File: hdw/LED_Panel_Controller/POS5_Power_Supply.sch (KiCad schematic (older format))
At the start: 20 parts

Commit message: lots of schematic progress
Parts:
- C?: display_footprint (none) -> 0402
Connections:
- net +5V: now also Q?.3 (D)
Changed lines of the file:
@@
 encoding utf-8
 Sheet 6 34
-Title "Pulse Oximeter"
-Date "2020-08-01"
+Title "LED Panel Controller"
+Date "2020-12-23"
 Rev "A"
-Comp "Drew Maatman"
+Comp "Drew Maatman, Logan Wedel"
 Comment1 ""
 Comment2 ""
@@
 F 2 "Capacitors_SMD:C_0402" H 4228 4620 50  0001 C CNN
 F 3 "" H 4215 4870 50  0001 C CNN
-F 4 "" H 4040 4870 50  0000 R CNN "display_footprint"
+F 4 "0402" H 4040 4870 50  0000 R CNN "display_footprint"
 F 5 "50V" H 4040 4770 50  0000 R CNN "Voltage"
 F 6 "X7R" H 4040 4670 50  0000 R CNN "Dielectric"
@@
 	-1   0    0    1
 $EndComp
+$Comp
+L power:+5V #PWR?
+U 1 1 5FE45BF8
+P 5120 7010
+F 0 "#PWR?" H 5120 6860 50  0001 C CNN
+F 1 "+5V" H 5120 7150 50  0000 C CNN
+F 2 "" H 5120 7010 50  0001 C CNN
+F 3 "" H 5120 7010 50  0001 C CNN
+	1    5120 7010
+	1    0    0    -1
+$EndComp
 $EndSCHEMATC

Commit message: made a lot more schematic progress
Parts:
- removed R?: 0.02, Resistors_SMD:R_0612, symbol Custom_Library:R_Custom
- removed R? (x2): 10, Resistors_SMD:R_0402, symbol Custom_Library:R_Custom
- added R? (x2): 10, Resistors_SMD:R_0402, symbol Custom_Library:R_Custom
- added R? (x3): 0, Resistors_SMD:R_0402, symbol Custom_Library:R_Custom
- added R?: 0.02, Resistors_SMD:R_0612, symbol Custom_Library:R_Custom
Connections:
- net +5V: now also R?.2, R?.2, R?.2, R?.2, R?.2
- net POS5_SNS_OUT+: now also R?.1
- net POS5_SNS_OUT-: now also R?.1
- net at C?.1, L?.2: now also R?.1, R?.1, R?.1, R?.1, R?.2

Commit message: more schematic development
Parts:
- removed C?: 100uF, symbol Custom_Library:C_Custom
- removed C?: 0.1uF, Capacitors_SMD:C_0402, symbol Custom_Library:C_Custom
- removed C?: 10uF, Capacitors_SMD:C_0402, symbol Custom_Library:C_Custom
- removed D?: BAT48JFILM, Diode_SMD:D_SOD-323, symbol Diode:BAT48JFILM
- removed L?: 2.2uH, symbol Custom_Library:L_Custom
- removed Q?: ZXMS6004FFTA, Package_TO_SOT_SMD:SOT-23, symbol Custom_Library:ZXMS6004FFTA
- removed Q?: BSS214NW, Package_TO_SOT_SMD:SOT-323_SC-70, symbol Transistor_FET:BSS214NW
- removed R?: 953k, Resistors_SMD:R_0402, symbol Custom_Library:R_Custom
- removed R? (x2): 10k, Resistors_SMD:R_0402, symbol Custom_Library:R_Custom
- removed R? (x2): 10, Resistors_SMD:R_0402, symbol Custom_Library:R_Custom
- removed R? (x3): 0, Resistors_SMD:R_0402, symbol Custom_Library:R_Custom
- removed R?: 0.02, Resistors_SMD:R_0612, symbol Custom_Library:R_Custom
- removed U?: TPS62130, Package_DFN_QFN:QFN-16-1EP_3x3mm_P0.5mm_EP1.8x1.8mm, symbol Custom_Library:TPS62130
- added C?: 0.1uF, Capacitors_SMD:C_0402, symbol Custom_Library:C_Custom
- added C? (x2): 10uF, Capacitors_SMD:C_1206, symbol Custom_Library:C_Custom
- added C?: 10uF, Capacitors_SMD:C_0402, symbol Custom_Library:C_Custom
- added D?: BAT48JFILM, Diode_SMD:D_SOD-323, symbol Diode:BAT48JFILM
- added L?: 2.2uH, symbol Custom_Library:L_Custom
- added Q?: ZXMS6004FFTA, Package_TO_SOT_SMD:SOT-23, symbol Custom_Library:ZXMS6004FFTA
- added Q?: BSS214NW, Package_TO_SOT_SMD:SOT-323_SC-70, symbol Transistor_FET:BSS214NW
- added R?: 0.02, Resistors_SMD:R_0612, symbol Custom_Library:R_Custom
- added R? (x2): 10, Resistors_SMD:R_0402, symbol Custom_Library:R_Custom
- added R? (x4): 0, Resistors_SMD:R_0402, symbol Custom_Library:R_Custom
- added R? (x3): 10k, Resistors_SMD:R_0402, symbol Custom_Library:R_Custom
- added R?: 953k, Resistors_SMD:R_0402, symbol Custom_Library:R_Custom
- added U?: 74LVC1G97, Package_TO_SOT_SMD:SOT-363_SC-70-6, symbol Custom_Library:74LVC1G97_Power_AND
- added U?: TPS62133, Package_DFN_QFN:QFN-16-1EP_3x3mm_P0.5mm_EP1.8x1.8mm, symbol Custom_Library:TPS62130
- C?: Dielectric X7R -> X5R; Digi-Key PN 1276-7031-1-ND -> 1276-1181-1-ND
- C?: Digi-Key PN (none) -> 490-10698-1-ND; Voltage 50V -> 25V
- C?: Digi-Key PN 490-13295-1-ND -> 399-3066-1-ND
- R?: Configuration (none) -> DNP; Digi-Key PN (none) -> RMCF0402FT180KCT-ND
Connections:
- net +12V: now also U?.10 (AVIN), U?.11 (PVIN), U?.12 (PVIN)
- net +3V3: now also R?.1, C?.1, D?.2 (A), U?.5 (VCC)
- net +5V: now also Q?.3 (D), R?.1, R?.2, R?.2, R?.2, R?.2, R?.2, U?.14 (VOS)
- net GND: now also C?.2, C?.2, C?.2, C?.2, Q?.2 (S), Q?.2 (S), R?.2, R?.2, R?.2, U?.1 (GND), U?.15 (PGND), U?.16 (PGND), U?.17 (EP), U?.2 (GND), U?.6 (AGND), U?.7 (FSW), U?.8 (DEF); no longer R?.2
- net POS5_PGOOD: now also R?.1, U?.4
- net POS5_RUN: now also Q?.1 (G), R?.1, U?.13 (EN), U?.3; no longer R?.1
- net at R?.1: now also R?.1, R?.2, U?.5 (FB)
- net at C?.1: now also U?.9 (SS/TR)
- new net: C?.1, C?.1, L?.2, R?.1, R?.1, R?.1, R?.1, R?.2
- new net: R?.2, U?.4 (PG), U?.6
- new net: L?.1, U?.1 (SW), U?.2 (SW), U?.3 (SW)
- new net: Q?.1 (G), Q?.3 (D), R?.2
- new net: C?.1, D?.1 (K), R?.1
- new net POS5_SNS+: R?.1
- new net POS5_SNS-: R?.1
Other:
- note added: "Fixed VOUT = +5V"
- moved on the sheet: R?, TP?

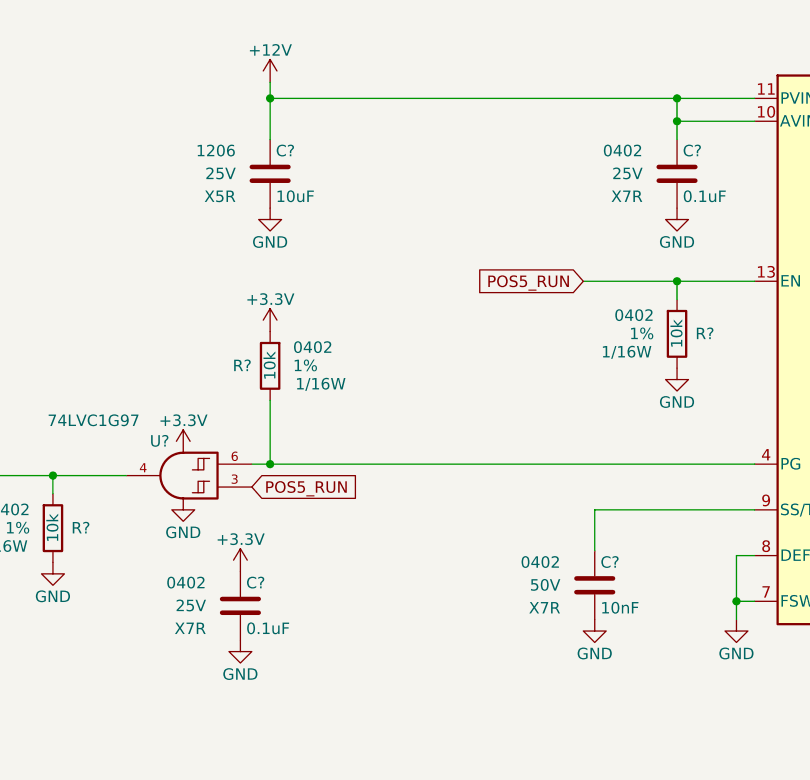
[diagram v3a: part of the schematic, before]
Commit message: added digikey pns, footprints, bom scrubbed
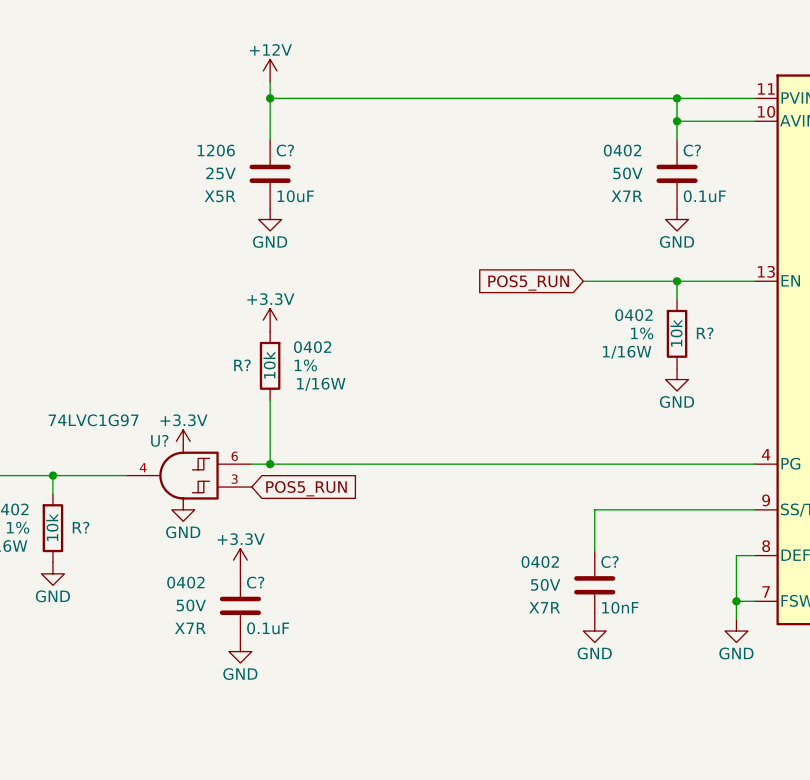
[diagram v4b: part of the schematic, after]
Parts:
- C? (x3): Digi-Key PN 1276-1181-1-ND -> 399-8153-1-ND
- C? (x2): Digi-Key PN 490-10698-1-ND -> 490-10701-1-ND; Voltage 25V -> 50V
- C?: Digi-Key PN 490-13211-1-ND -> 1276-1451-1-ND
- L?: footprint (none) -> Inductors_SMD:L_Vishay_IHLP-2020
- R? (x4): Digi-Key PN 2019-RK73Z1ETTPCT-ND -> RMCF0402ZT0R00CT-ND
- R?: Digi-Key PN (none) -> RMCF0402FT953KCT-ND
- U?: Digi-Key PN 296-SN74LVC1G97DCK3CT-ND -> 1727-1772-1-ND
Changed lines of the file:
@@
 F 3 "" H 4575 3070 50  0001 C CNN
 F 4 "0402" H 4400 3070 50  0000 R CNN "display_footprint"
-F 5 "25V" H 4400 2970 50  0000 R CNN "Voltage"
+F 5 "50V" H 4400 2970 50  0000 R CNN "Voltage"
 F 6 "X7R" H 4400 2870 50  0000 R CNN "Dielectric"
-F 7 "490-10698-1-ND" H 4550 2970 50  0001 C CNN "Digi-Key PN"
+F 7 "490-10701-1-ND" H 4550 2970 50  0001 C CNN "Digi-Key PN"
 	1    4550 2970
 	1    0    0    -1
@@
 F 5 "25V" H 2620 2970 50  0000 R CNN "Voltage"
 F 6 "X5R" H 2620 2870 50  0000 R CNN "Dielectric"
-F 7 "1276-1181-1-ND" H 3195 3470 60  0001 C CNN "Digi-Key PN"
+F 7 "399-8153-1-ND" H 3195 3470 60  0001 C CNN "Digi-Key PN"
 	1    2770 2970
 	1    0    0    -1
@@
 F 2 "Package_TO_SOT_SMD:SOT-363_SC-70-6" H 2440 4290 50  0001 C CNN
 F 3 "http://www.ti.com/lit/ds/symlink/sn74lvc1g97.pdf" H 2440 4290 50  0001 C CNN
-F 4 "296-SN74LVC1G97DCK3CT-ND" H 2390 4290 50  0001 C CNN "Digi-Key PN"
+F 4 "1727-1772-1-ND" H 2390 4290 50  0001 C CNN "Digi-Key PN"
 	1    2390 4290
 	-1   0    0    -1
@@
 F 3 "" H 2665 4960 50  0001 C CNN
 F 4 "0402" H 2490 4960 50  0000 R CNN "display_footprint"
-F 5 "25V" H 2490 4860 50  0000 R CNN "Voltage"
+F 5 "50V" H 2490 4860 50  0000 R CNN "Voltage"
 F 6 "X7R" H 2490 4760 50  0000 R CNN "Dielectric"
-F 7 "490-10698-1-ND" H 2640 4860 50  0001 C CNN "Digi-Key PN"
+F 7 "490-10701-1-ND" H 2640 4860 50  0001 C CNN "Digi-Key PN"
 	1    2640 4860
 	1    0    0    -1
@@
 F 5 "1%" H 7310 4720 50  0000 R CNN "Tolerance"
 F 6 "1/16W" H 7310 4620 50  0000 R CNN "Wattage"
-F 7 "2019-RK73Z1ETTPCT-ND" H 7410 4720 50  0001 C CNN "Digi-Key PN"
+F 7 "RMCF0402ZT0R00CT-ND" H 7410 4720 50  0001 C CNN "Digi-Key PN"
 	1    7410 4720
 	-1   0    0    -1
@@
 F 6 "1/16W" V 8310 3450 50  0001 C CNN "Wattage"
 F 7 "~Telemetry" V 8110 3450 50  0000 C CNN "Configuration"
-F 8 "2019-RK73Z1ETTPCT-ND" H 8010 3450 50  0001 C CNN "Digi-Key PN"
+F 8 "RMCF0402ZT0R00CT-ND" H 8010 3450 50  0001 C CNN "Digi-Key PN"
 	1    8010 3450
 	0    -1   1    0
@@
 F 6 "1/16W" V 8310 3750 50  0001 C CNN "Wattage"
 F 7 "~Telemetry" V 8110 3750 50  0000 C CNN "Configuration"
-F 8 "2019-RK73Z1ETTPCT-ND" H 8010 3750 50  0001 C CNN "Digi-Key PN"
+F 8 "RMCF0402ZT0R00CT-ND" H 8010 3750 50  0001 C CNN "Digi-Key PN"
 	1    8010 3750
 	0    -1   1    0
@@
 F 6 "1/16W" V 8310 4050 50  0001 C CNN "Wattage"
 F 7 "~Telemetry" V 8110 4050 50  0000 C CNN "Configuration"
-F 8 "2019-RK73Z1ETTPCT-ND" H 8010 4050 50  0001 C CNN "Digi-Key PN"
+F 8 "RMCF0402ZT0R00CT-ND" H 8010 4050 50  0001 C CNN "Digi-Key PN"
 	1    8010 4050
 	0    -1   1    0
@@
 F 5 "25V" H 7260 3280 50  0000 R CNN "Voltage"
 F 6 "X5R" H 7260 3180 50  0000 R CNN "Dielectric"
-F 7 "1276-1181-1-ND" H 7835 3780 60  0001 C CNN "Digi-Key PN"
+F 7 "399-8153-1-ND" H 7835 3780 60  0001 C CNN "Digi-Key PN"
 	1    7410 3280
 	1    0    0    -1
@@
 F 5 "25V" H 6670 3280 50  0000 R CNN "Voltage"
 F 6 "X5R" H 6670 3180 50  0000 R CNN "Dielectric"
-F 7 "1276-1181-1-ND" H 7245 3780 60  0001 C CNN "Digi-Key PN"
+F 7 "399-8153-1-ND" H 7245 3780 60  0001 C CNN "Digi-Key PN"
 	1    6820 3280
 	1    0    0    -1
@@
 F 0 "L?" V 6280 3040 50  0000 C CNN
 F 1 "2.2uH" V 6405 3040 50  0000 C CNN
-F 2 "" H 6330 3040 50  0001 C CNN
+F 2 "Inductors_SMD:L_Vishay_IHLP-2020" H 6330 3040 50  0001 C CNN
 F 3 "" H 6330 3040 50  0001 C CNN
 F 4 "IHLP2020" V 6480 3040 50  0000 C CNN "display_footprint"
@@
 F 6 "1/16W" H 8820 3730 50  0000 L CNN "Wattage"
 F 7 "DNP" H 8560 3890 50  0000 C CNN "Configuration"
+F 8 "RMCF0402FT953KCT-ND" H 8710 3810 50  0001 C CNN "Digi-Key PN"
 	1    8710 3810
 	1    0    0    -1
@@
 F 5 "6.3V" H 3220 6850 50  0000 R CNN "Voltage"
 F 6 "X5R" H 3220 6750 50  0000 R CNN "Dielectric"
-F 7 "490-13211-1-ND" H 3370 6850 50  0001 C CNN "Digi-Key PN"
+F 7 "1276-1451-1-ND" H 3370 6850 50  0001 C CNN "Digi-Key PN"
 	1    3370 6850
 	1    0    0    -1

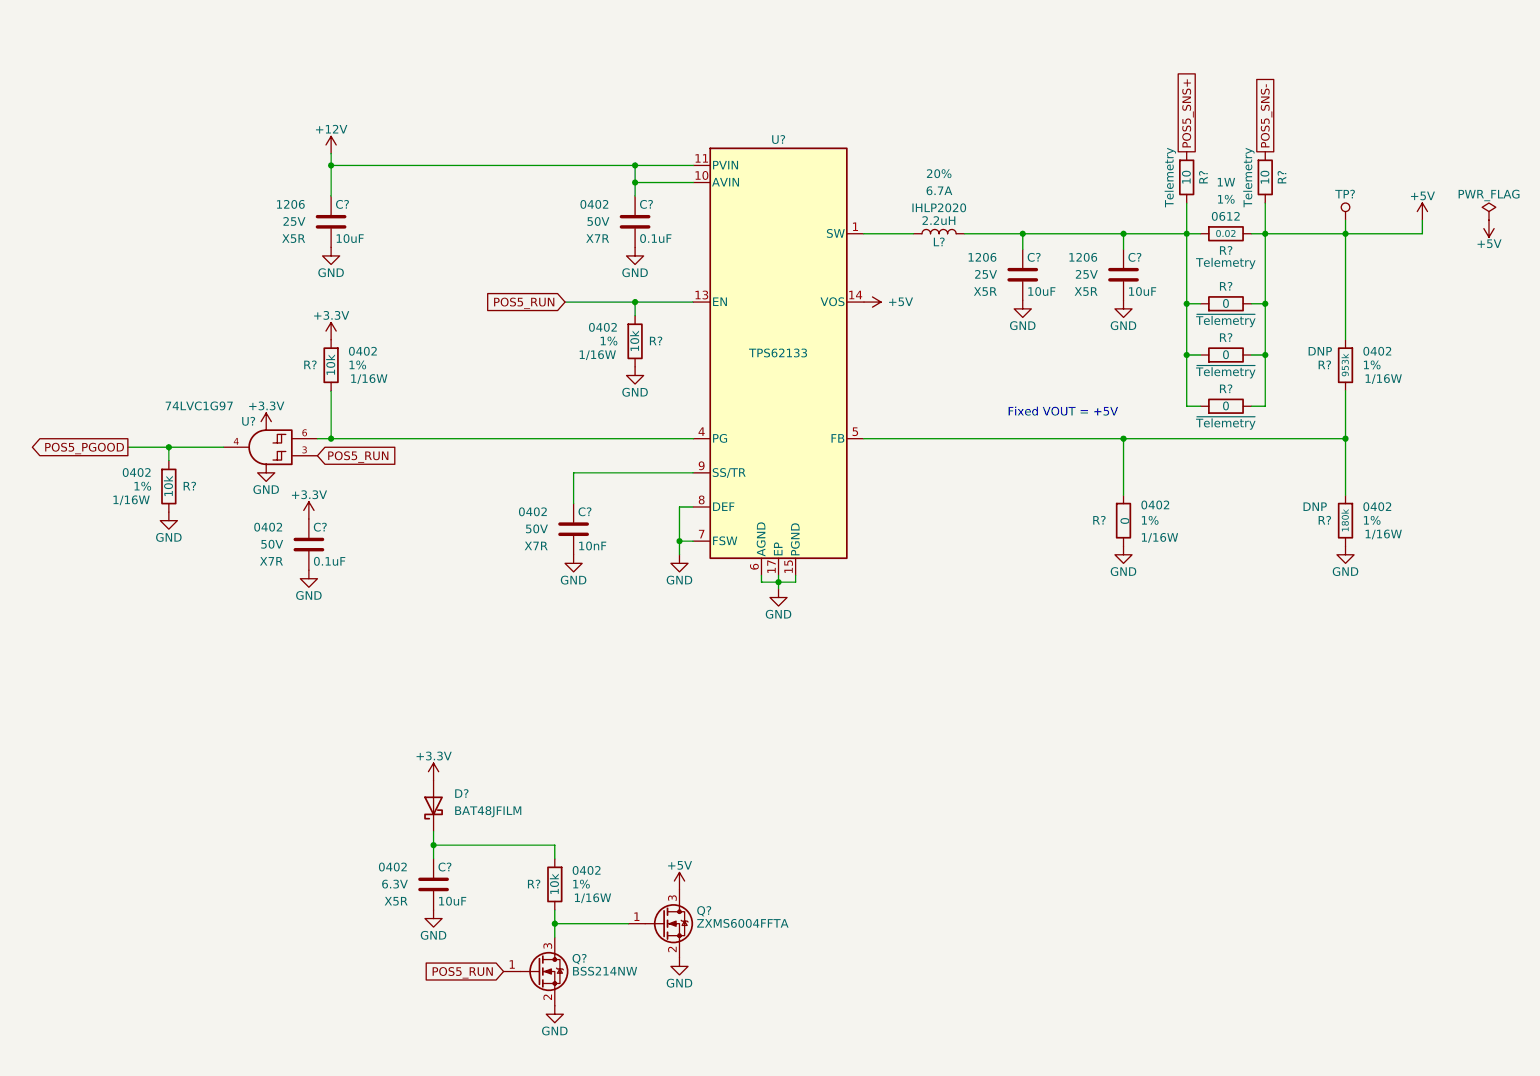
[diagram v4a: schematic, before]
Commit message: assigned I2C addresses
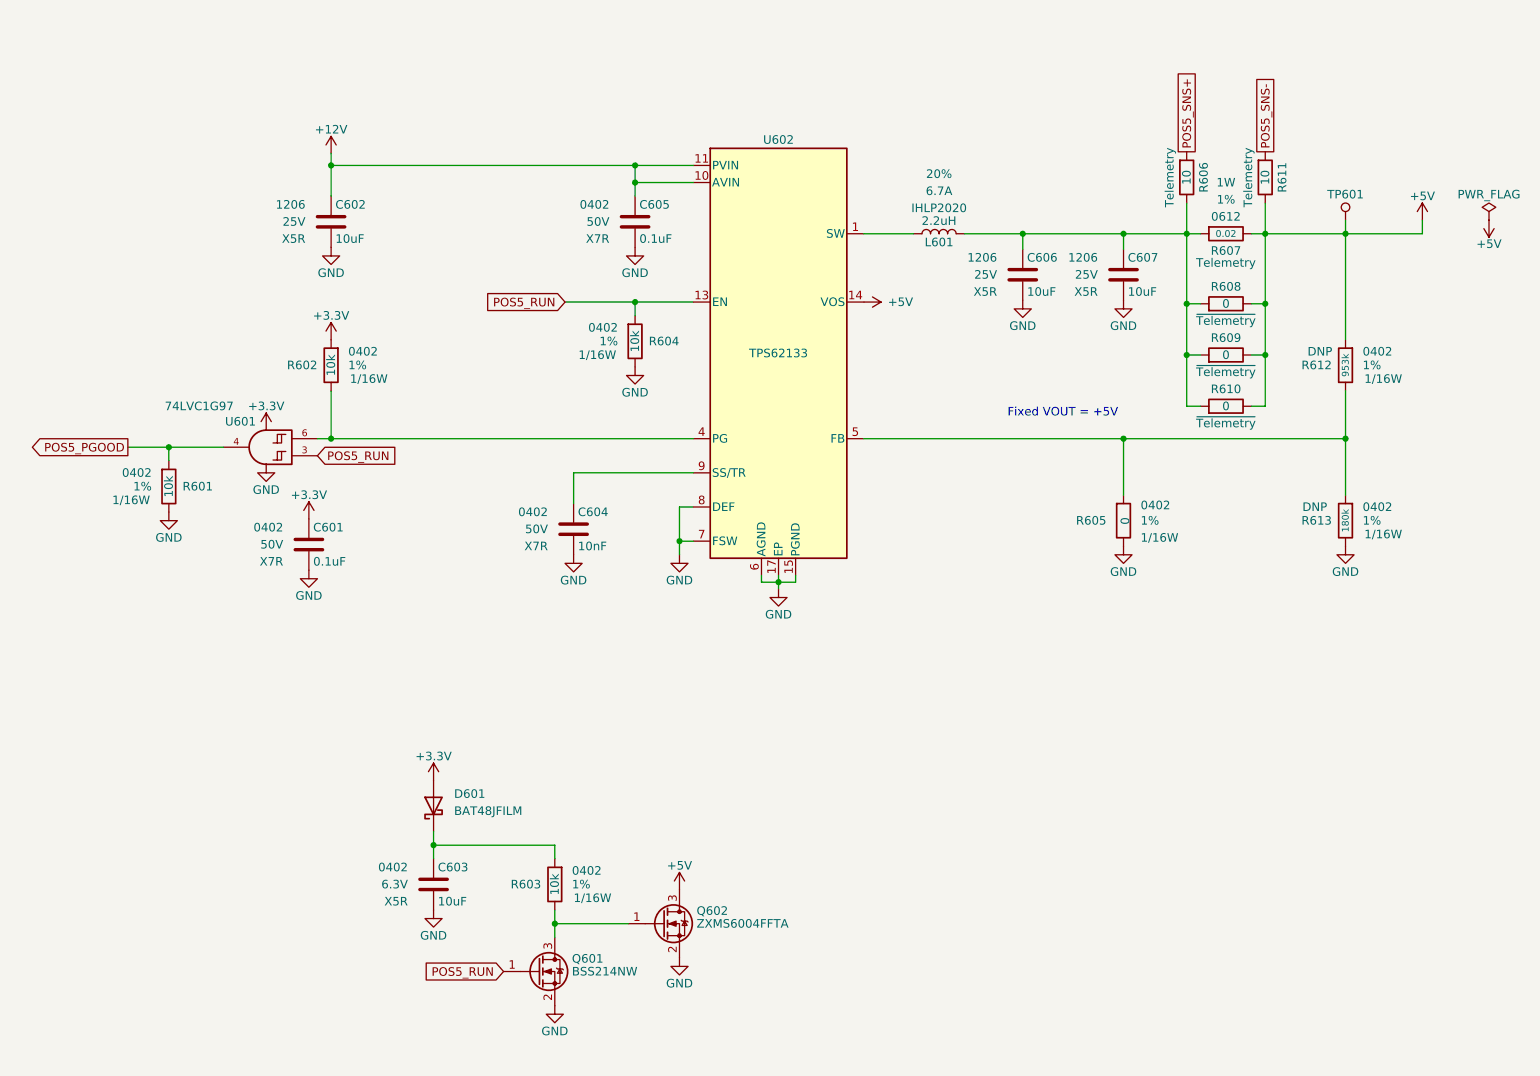
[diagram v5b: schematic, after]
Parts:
- removed C? (x2): 10uF, Capacitors_SMD:C_1206, symbol Custom_Library:C_Custom
- removed C?: 10nF, Capacitors_SMD:C_0402, symbol Custom_Library:C_Custom
- removed C?: 0.1uF, Capacitors_SMD:C_0402, symbol Custom_Library:C_Custom
- removed R?: 10, Resistors_SMD:R_0402, symbol Custom_Library:R_Custom
- removed R?: 10k, Resistors_SMD:R_0402, symbol Custom_Library:R_Custom
- added C601: 0.1uF, Capacitors_SMD:C_0402, symbol Custom_Library:C_Custom
- added C602, C606: 10uF, Capacitors_SMD:C_1206, symbol Custom_Library:C_Custom
- added C604: 10nF, Capacitors_SMD:C_0402, symbol Custom_Library:C_Custom
- added R601: 10k, Resistors_SMD:R_0402, symbol Custom_Library:R_Custom
- added R611: 10, Resistors_SMD:R_0402, symbol Custom_Library:R_Custom
- gave numbers to parts that had none: 21
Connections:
- net +12V: now also C602.1
- net +3V3: now also C601.1
- net +5V: now also R611.2
- net GND: now also C601.2, C602.2, C604.2, C606.2, R601.2
- net POS5_PGOOD: now also R601.1
- net POS5_SNS-: now also R611.1
- net at C607.1, L601.2, R606.2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: now also C606.1
- net at U602.9 (SS/TR): now also C604.1

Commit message: added BOMs, some consolidation
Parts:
- C601, C605: Digi-Key PN 490-10701-1-ND -> 490-10698-1-ND
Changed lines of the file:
@@
 F 5 "50V" H 4400 2970 50  0000 R CNN "Voltage"
 F 6 "X7R" H 4400 2870 50  0000 R CNN "Dielectric"
-F 7 "490-10701-1-ND" H 4550 2970 50  0001 C CNN "Digi-Key PN"
+F 7 "490-10698-1-ND" H 4550 2970 50  0001 C CNN "Digi-Key PN"
 	1    4550 2970
 	1    0    0    -1
@@
 F 5 "50V" H 2490 4860 50  0000 R CNN "Voltage"
 F 6 "X7R" H 2490 4760 50  0000 R CNN "Dielectric"
-F 7 "490-10701-1-ND" H 2640 4860 50  0001 C CNN "Digi-Key PN"
+F 7 "490-10698-1-ND" H 2640 4860 50  0001 C CNN "Digi-Key PN"
 	1    2640 4860
 	1    0    0    -1
